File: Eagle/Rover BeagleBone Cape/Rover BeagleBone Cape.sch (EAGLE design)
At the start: 31 parts, among them IC1 TXB0108TSSOP, IC2 VREG-3TO-263, M0 M-1X05PTH, M1 M-1X05PTH, M2 M-1X05PTH, M3 M-1X05PTH, M4 M-1X05PTH, M5 M-1X05PTH, U2 MCP9808MSOP, U3 HTU21DSMD, U4 BMP180, U6 Hydrogen, U7 Carbon Monoxide, U8 LPG, U9 Methane

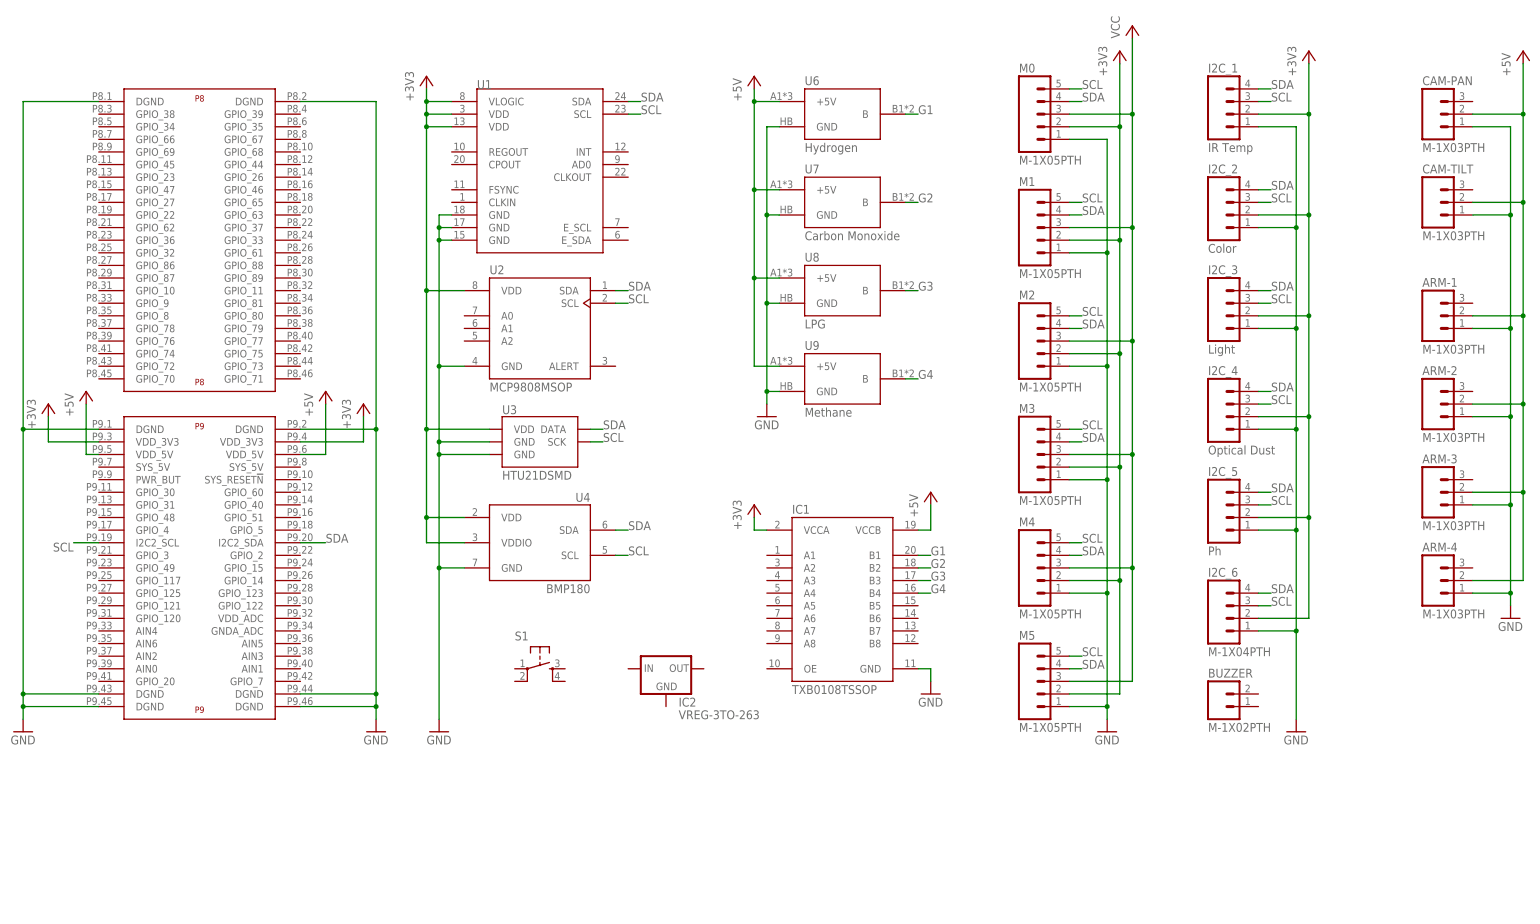
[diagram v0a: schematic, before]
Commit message: Added preliminary motor controller code
Added Arduino code and PCB revisions
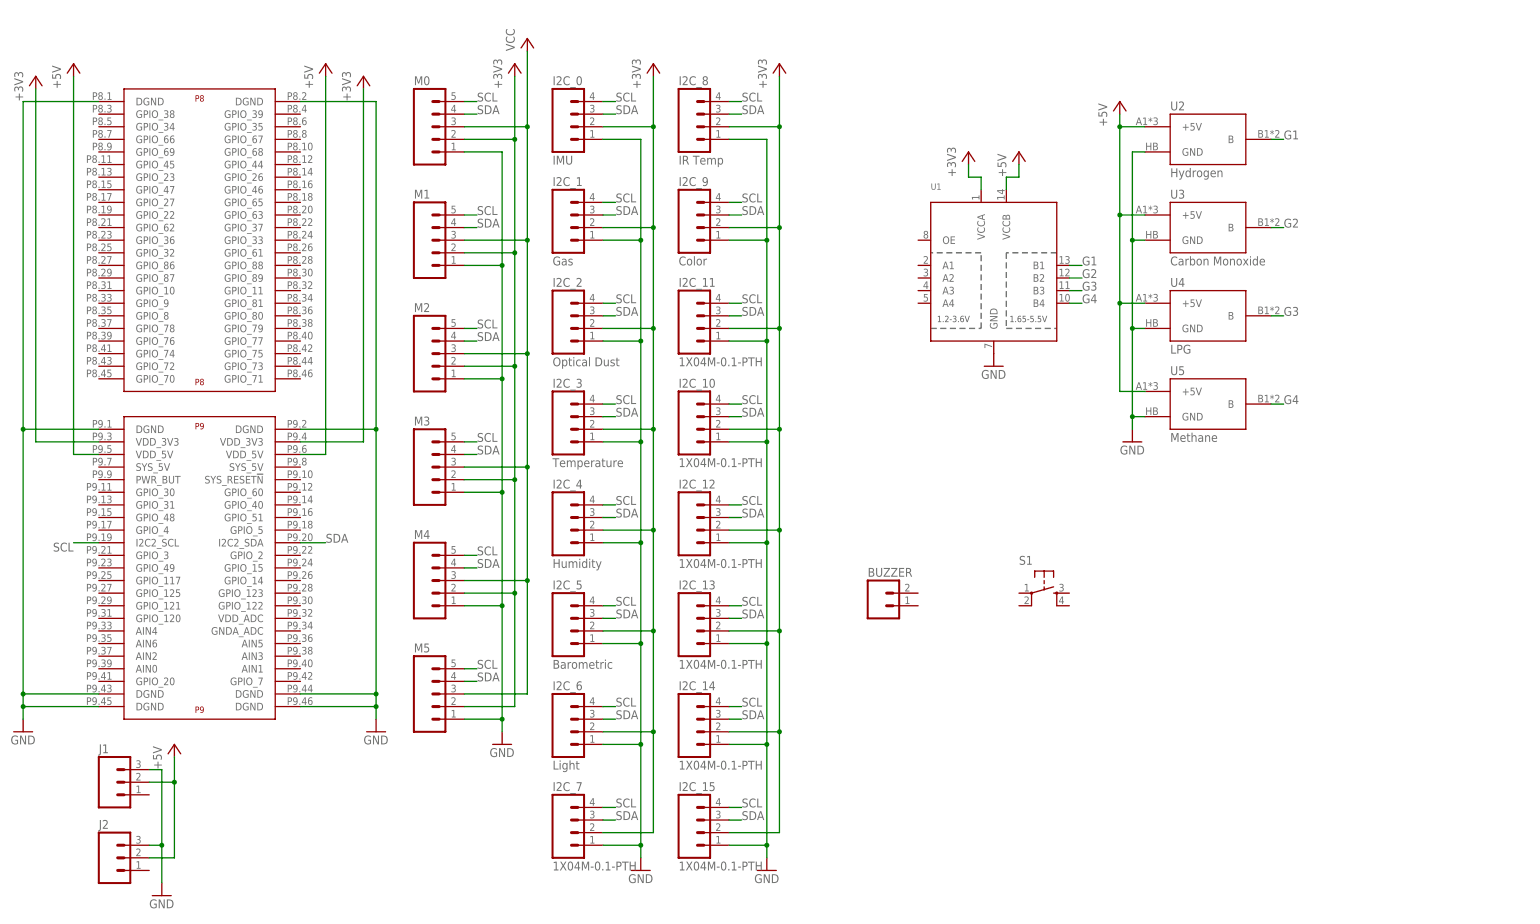
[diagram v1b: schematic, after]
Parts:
- removed ARM-1, ARM-2, ARM-3, ARM-4, CAM-PAN, CAM-TILT: M-1X03PTH, Jordi:M-1X03PTH
- removed IC1: TXB0108TSSOP, Jordi:TXB0108TSSOP
- removed IC2: VREG-3TO-263, Jordi:VREG-3TO-263
- removed U6: Hydrogen, Jordi:GAS-SENSORMQ
- removed U7: Carbon Monoxide, Jordi:GAS-SENSORMQ
- removed U8: LPG, Jordi:GAS-SENSORMQ
- removed U9: Methane, Jordi:GAS-SENSORMQ
- added I2C_0: IMU, Jordi:1X04M-0.1-PTH
- added I2C_10, I2C_11, I2C_12, I2C_13, I2C_14, I2C_15, I2C_7: 1X04M-0.1-PTH, Jordi:1X04M-0.1-PTH
- added I2C_8: IR Temp, Jordi:1X04M-0.1-PTH
- added I2C_9: Color, Jordi:1X04M-0.1-PTH
- added J1, J2: (no value), Jordi:1X03M-0.1-PTH
- added U5: Methane, Jordi:GAS-SENSORMQ
- BUZZER: value M-1X02PTH -> (none); device Jordi:M-1X02PTH -> Jordi:1X02M-0.1-PTH
- I2C_1: value IR Temp -> Gas; device Jordi:M-1X04PTH -> Jordi:1X04M-0.1-PTH
- I2C_2: value Color -> Optical Dust; device Jordi:M-1X04PTH -> Jordi:1X04M-0.1-PTH
- I2C_3: value Light -> Temperature; device Jordi:M-1X04PTH -> Jordi:1X04M-0.1-PTH
- I2C_4: value Optical Dust -> Humidity; device Jordi:M-1X04PTH -> Jordi:1X04M-0.1-PTH
- I2C_5: value Ph -> Barometric; device Jordi:M-1X04PTH -> Jordi:1X04M-0.1-PTH
- I2C_6: value M-1X04PTH -> Light; device Jordi:M-1X04PTH -> Jordi:1X04M-0.1-PTH
- M0, M1, M2, M3, M4, M5: value M-1X05PTH -> (none); device Jordi:M-1X05PTH -> Jordi:1X05M-0.1-PTH
- U1: device SparkFun-Sensors:MPU-9150QFN-24-NP -> SparkFun-DigitalIC:TXB0104PWR
- U2: value MCP9808MSOP -> Hydrogen; device Jordi:MCP9808MSOP -> Jordi:GAS-SENSORMQ
- U3: value HTU21DSMD -> Carbon Monoxide; device SparkFun-Sensors:HTU21DSMD -> Jordi:GAS-SENSORMQ
- U4: value BMP180 -> LPG; device SparkFun-Sensors:BMP180 -> Jordi:GAS-SENSORMQ
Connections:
- net +3V3: now also I2C_0.2, I2C_10.2, I2C_11.2, I2C_12.2, I2C_13.2, I2C_14.2, I2C_15.2, I2C_7.2, I2C_8.2, I2C_9.2, U1.VCCA; no longer IC1.VCCA, U1.VDD@13, U1.VDD@3, U1.VLOGIC, U2.VDD, U3.VDD, U4.VDD, U4.VDDIO
- net +5V: now also J1.2, J2.2, U1.VCCB, U2.+5V, U3.+5V, U4.+5V, U5.+5V; no longer ARM-1.2, ARM-2.2, ARM-3.2, ARM-4.2, CAM-PAN.2, CAM-TILT.2, IC1.VCCB, U6.+5V, U7.+5V, U8.+5V, U9.+5V
- net G1: now also U1.B1, U2.B; no longer IC1.B1, U6.B
- net G2: now also U1.B2, U3.B; no longer IC1.B2, U7.B
- net G3: now also U1.B3, U4.B; no longer IC1.B3, U8.B
- net G4: now also U1.B4, U5.B; no longer IC1.B4, U9.B
- net GND: now also I2C_0.1, I2C_10.1, I2C_11.1, I2C_12.1, I2C_13.1, I2C_14.1, I2C_15.1, I2C_7.1, I2C_8.1, I2C_9.1, J1.3, J2.3, U1.GND, U3.GND, U5.GND; no longer ARM-1.1, ARM-2.1, ARM-3.1, ARM-4.1, CAM-PAN.1, CAM-TILT.1, IC1.GND, U1.GND@15, U1.GND@17, U1.GND@18, U3.GND@2, U3.GND@7, U6.GND, U7.GND, U8.GND, U9.GND
- net SCL: now also I2C_0.4, I2C_1.4, I2C_10.4, I2C_11.4, I2C_12.4, I2C_13.4, I2C_14.4, I2C_15.4, I2C_2.4, I2C_3.4, I2C_4.4, I2C_5.4, I2C_6.4, I2C_7.4, I2C_8.4, I2C_9.4; no longer I2C_1.3, I2C_2.3, I2C_3.3, I2C_4.3, I2C_5.3, I2C_6.3, U1.SCL, U2.SCL, U3.SCK, U4.SCL
- net SDA: now also I2C_0.3, I2C_1.3, I2C_10.3, I2C_11.3, I2C_12.3, I2C_13.3, I2C_14.3, I2C_15.3, I2C_2.3, I2C_3.3, I2C_4.3, I2C_5.3, I2C_6.3, I2C_7.3, I2C_8.3, I2C_9.3; no longer I2C_1.4, I2C_2.4, I2C_3.4, I2C_4.4, I2C_5.4, I2C_6.4, U1.SDA, U2.SDA, U3.DATA, U4.SDA
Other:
- moved on the sheet: BUZZER, I2C_1, I2C_2, I2C_3, I2C_4, I2C_5, I2C_6, M0, M1, M2, M3, M4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
